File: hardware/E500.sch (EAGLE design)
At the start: 27 parts, among them SW1 SPST_TACT-KMR2, U11 915MHz, U5 ATMEGA328P-MU, U8 MCP1703CB, X1 16 MHz

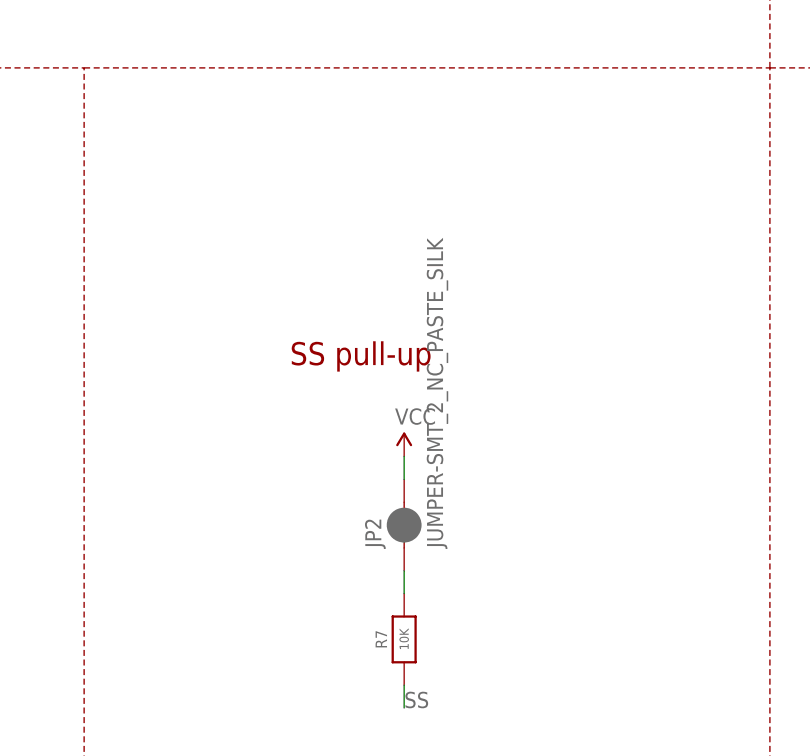
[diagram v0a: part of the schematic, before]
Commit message: v2.2 - minor update
- removed solder jumper from SS pin
- added bottom silkscreen for node id
- DRU mask limit to 14mil for covering via with solder mask
- very minor trace adjustment
- functionally same as previous
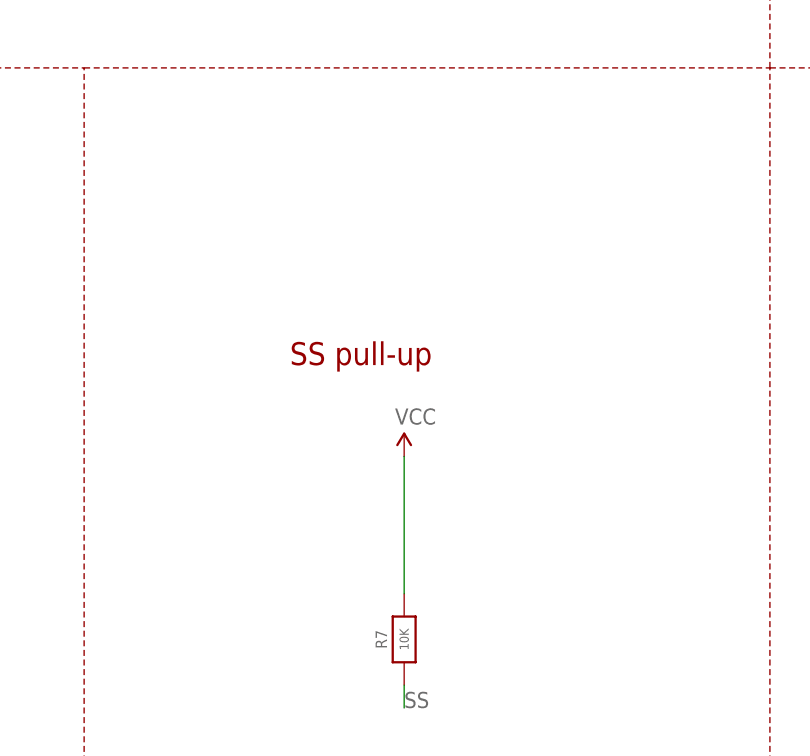
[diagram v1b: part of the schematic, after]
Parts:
- removed JP2: JUMPER-SMT_2_NC_PASTE_SILK, SparkFun-Jumpers:JUMPER-SMT_2_NC_PASTE_SILK
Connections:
- removed net N$11: JP2.1, R7.2
- net VCC: now also R7.2; no longer JP2.2
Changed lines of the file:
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@@
 <?xml version="1.0" encoding="utf-8"?>
 <!DOCTYPE eagle SYSTEM "eagle.dtd">
-<eagle version="9.4.1">
+<eagle version="9.5.1">
 <drawing>
 <settings>
@@
 <part name="GND11" library="SparkFun-Aesthetics" deviceset="GND" device=""/>
 <part name="SUPPLY2" library="SparkFun-Aesthetics" deviceset="VCC" device=""/>
-<part name="JP2" library="SparkFun-Jumpers" library_urn="urn:adsk.eagle:library:528" deviceset="JUMPER-SMT_2_NC_PASTE" device="_SILK" package3d_urn="urn:adsk.eagle:package:39282/1"/>
 <part name="D1" library="SCHOTTKY_0805" deviceset="DIODE_SCHOTTKY" device="0805-RES"/>
 <part name="GND4" library="supply1" library_urn="urn:adsk.eagle:library:371" deviceset="GND" device=""/>
@@
 <attribute name="VALUE" x="209.804" y="49.276" size="1.778" layer="96"/>
 </instance>
-<instance part="JP2" gate="G$1" x="210.82" y="38.1" smashed="yes" rot="R90">
-<attribute name="NAME" x="208.28" y="35.56" size="1.778" layer="95" font="vector" rot="R90"/>
-<attribute name="VALUE" x="213.36" y="35.56" size="1.778" layer="96" font="vector" rot="R90" align="top-left"/>
-</instance>
 <instance part="D1" gate="G$1" x="137.16" y="-63.5" smashed="yes">
 <attribute name="NAME" x="133.35" y="-61.7474" size="1.778" layer="95"/>
@@
 </segment>
 <segment>
-<wire x1="210.82" y1="43.18" x2="210.82" y2="45.72" width="0.1524" layer="91"/>
-<pinref part="SUPPLY2" gate="G$1" pin="VCC"/>
-<pinref part="JP2" gate="G$1" pin="2"/>
-</segment>
-<segment>
 <wire x1="154.94" y1="43.18" x2="154.94" y2="48.26" width="0.1524" layer="91"/>
 <pinref part="SUPPLY5" gate="G$1" pin="VCC"/>
 <wire x1="154.94" y1="35.56" x2="154.94" y2="43.18" width="0.1524" layer="91"/>
 <pinref part="J2" gate="G$1" pin="1"/>
+</segment>
+<segment>
+<pinref part="R7" gate="G$1" pin="2"/>
+<pinref part="SUPPLY2" gate="G$1" pin="VCC"/>
+<wire x1="210.82" y1="30.48" x2="210.82" y2="45.72" width="0.1524" layer="91"/>
 </segment>
 </net>
@@
 </segment>
 </net>
-<net name="N$11" class="0">
-<segment>
-<pinref part="R7" gate="G$1" pin="2"/>
-<wire x1="210.82" y1="30.48" x2="210.82" y2="33.02" width="0.1524" layer="91"/>
-<pinref part="JP2" gate="G$1" pin="1"/>
-</segment>
-</net>
